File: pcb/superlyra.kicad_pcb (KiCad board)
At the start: 2 copper layers, 391.1 x 134.8 mm, 224 parts, among them J1 USB_C_Receptacle_USB2.0, J2 AVR-ISP-6, SW1 SW_Push, SW10 SW_Push, SW11 SW_Push, SW12 SW_Push, SW13 SW_Push, SW14 SW_Push, SW15 SW_Push, SW16 SW_Push, SW17 SW_Push, SW18 SW_Push, SW19 SW_Push, SW2 SW_Push, SW20 SW_Push, SW21 SW_Push, SW22 SW_Push, SW23 SW_Push, SW24 SW_Push, SW25 SW_Push, SW26 SW_Push, SW27 SW_Push, SW28 SW_Push, SW29 SW_Push, SW3 SW_Push, SW30 SW_Push, SW31 SW_Push, SW32 SW_Push, SW33 SW_Push, SW34 SW_Push, SW35 SW_Push, SW36 SW_Push, SW37 SW_Push, SW38 SW_Push, SW39 SW_Push, SW4 SW_Push, SW40 SW_Push, SW41 SW_Push, SW42 SW_Push, SW43 SW_Push, SW44 SW_Push, SW45 SW_Push, SW46 SW_Push, SW47 SW_Push, SW48 SW_Push, SW49 SW_Push, SW5 SW_Push, SW50 SW_Push, SW51 SW_Push, SW52 SW_Push, SW53 SW_Push, SW54 SW_Push, SW55 SW_Push, SW56 SW_Push, SW57 SW_Push, SW58 SW_Push, SW59 SW_Push, SW6 SW_Push, SW60 SW_Push, SW61 SW_Push, SW62 SW_Push, SW63 SW_Push, SW64 SW_Push, SW65 SW_Push, SW66 SW_Push, SW67 SW_Push, SW68 SW_Push, SW69 SW_Push, SW7 SW_Push, SW70 SW_Push, SW71 SW_Push, SW72 SW_Push, SW73 SW_Push, SW74 SW_Push, SW75 SW_Push, SW76 SW_Push, SW77 SW_Push, SW78 SW_Push, SW79 SW_Push, SW8 SW_Push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

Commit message: lots, see list
- Added a power plane under the MCU
- moved the CC resistors incase hand soldering is required
- moved a via that was overlapping a different net trace
- sorted DRC some DRC errors, mainly courtyard overlaps
- added smol Easter egg
- made some traces around the MCU slightly prettier.
- probably something else
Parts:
- moved R5 2.89 mm to (214.9, 84.5)
- moved R6 2.86 mm to (204.9, 84.5)
- moved C3 2.30 mm to (243.2, 82.8), turned to 45 degrees
- moved C2 1.28 mm to (238.8, 78.3), turned to 45 degrees
- moved C4 0.80 mm to (238.0, 90.8), turned to 225 degrees
- moved R4 0.49 mm to (243.2, 86.4), turned to 135 degrees
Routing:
- net VCC: track 108.0 -> 86.9 mm
- net GND: track 57.9 -> 62.9 mm
- net Net-(J1-PadA5): track 1.41 -> 4.61 mm
- net Net-(J1-PadB5): track 1.36 -> 3.94 mm
- net DI-: track 32.6 -> 33.5 mm
- added copper zone on F.Cu, net /vbus-in
- added copper zone on B.Cu, net VCC
- added copper zone on F.Cu, net VCC
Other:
- board text added: "Envious was here"

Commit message: added lables for the reset button and ISP header. moved all references to cmts instead of silkscreen as it looks neater.,
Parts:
- moved C1 0.53 mm to (235.9, 78.7), turned to 45 degrees
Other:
- board text added: "GND"
- board text added: "MISO"
- board text added: "MOSI"
- board text added: "RESET MCU"
- board text added: "RST"
- board text added: "SCK"
- board text added: "VCC"

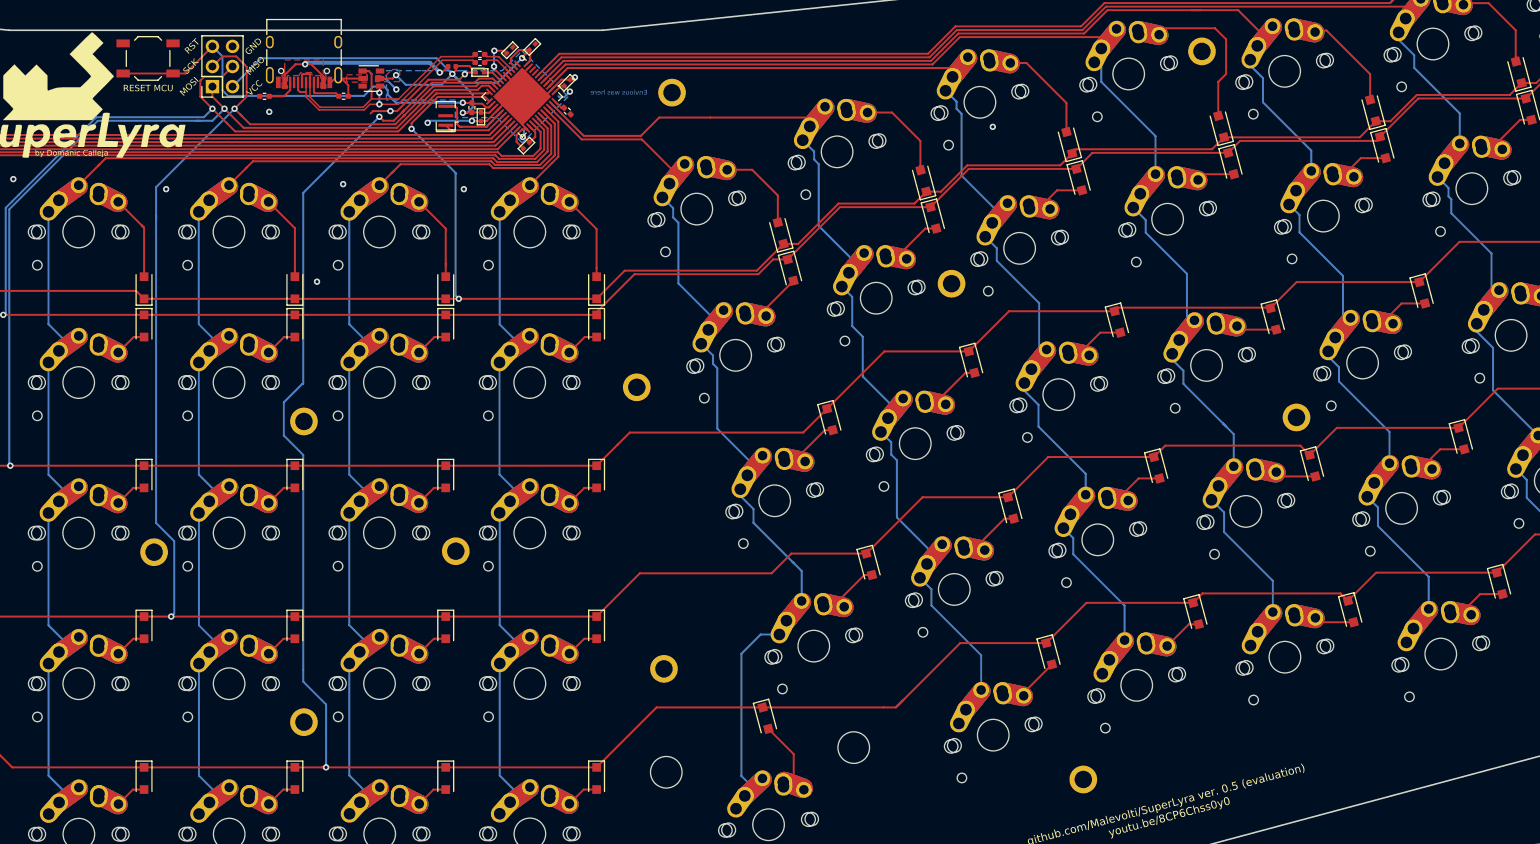
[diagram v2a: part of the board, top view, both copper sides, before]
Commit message: Moved all the traces I could find away from holes and edges to account for mechanical damage.
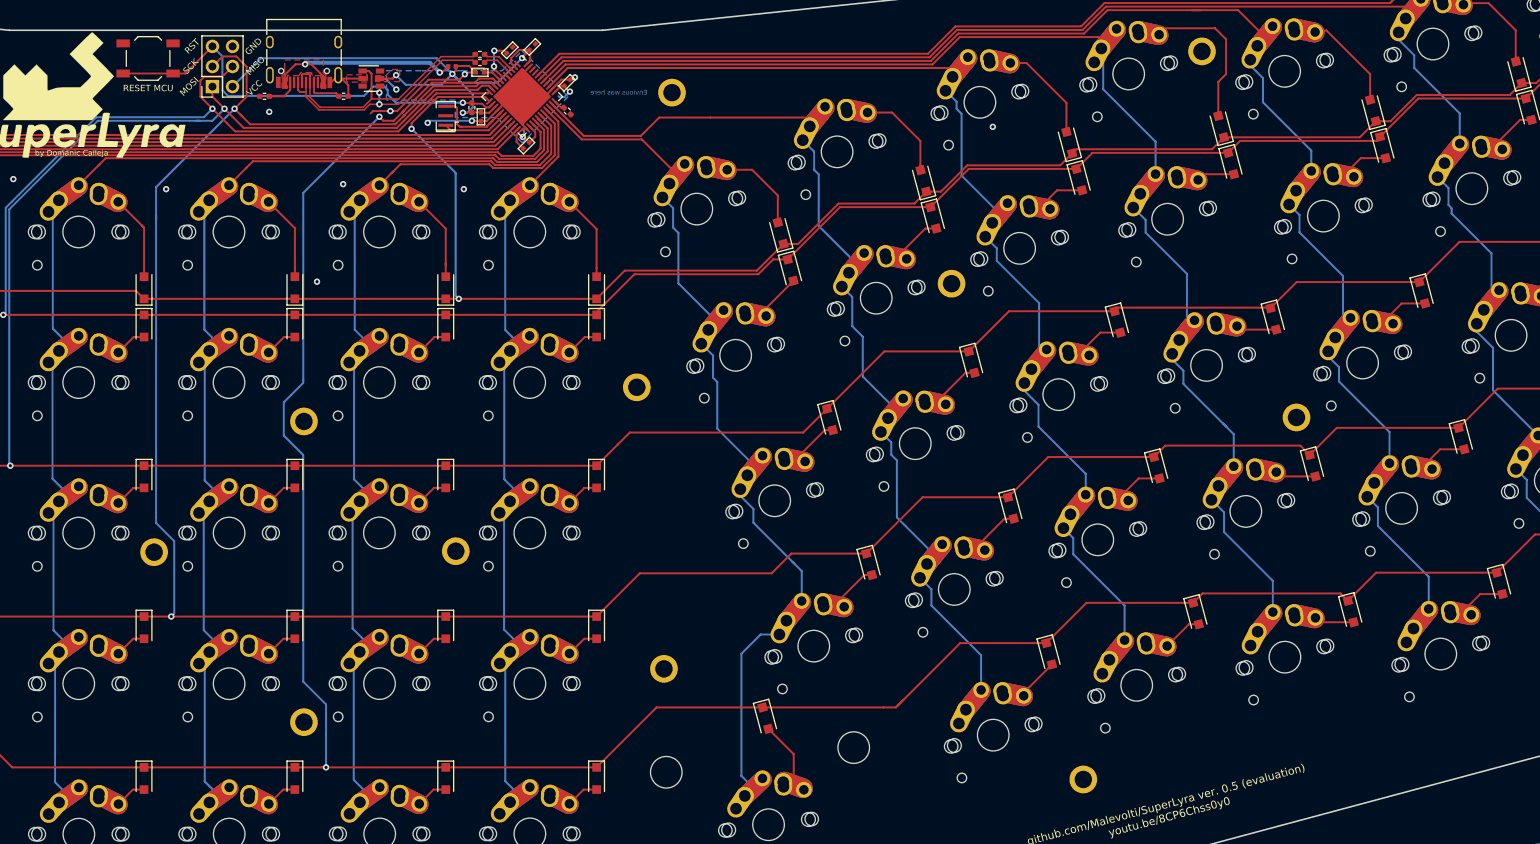
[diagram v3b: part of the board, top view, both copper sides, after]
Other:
- net class Default: clearance 0.127 -> 0.2
- rule trace_clearance: 0.127 -> 0.2
